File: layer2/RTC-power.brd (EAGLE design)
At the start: 17.8 x 49.5 mm, 14 parts, among them U1 DS3234, U2 MCP73831

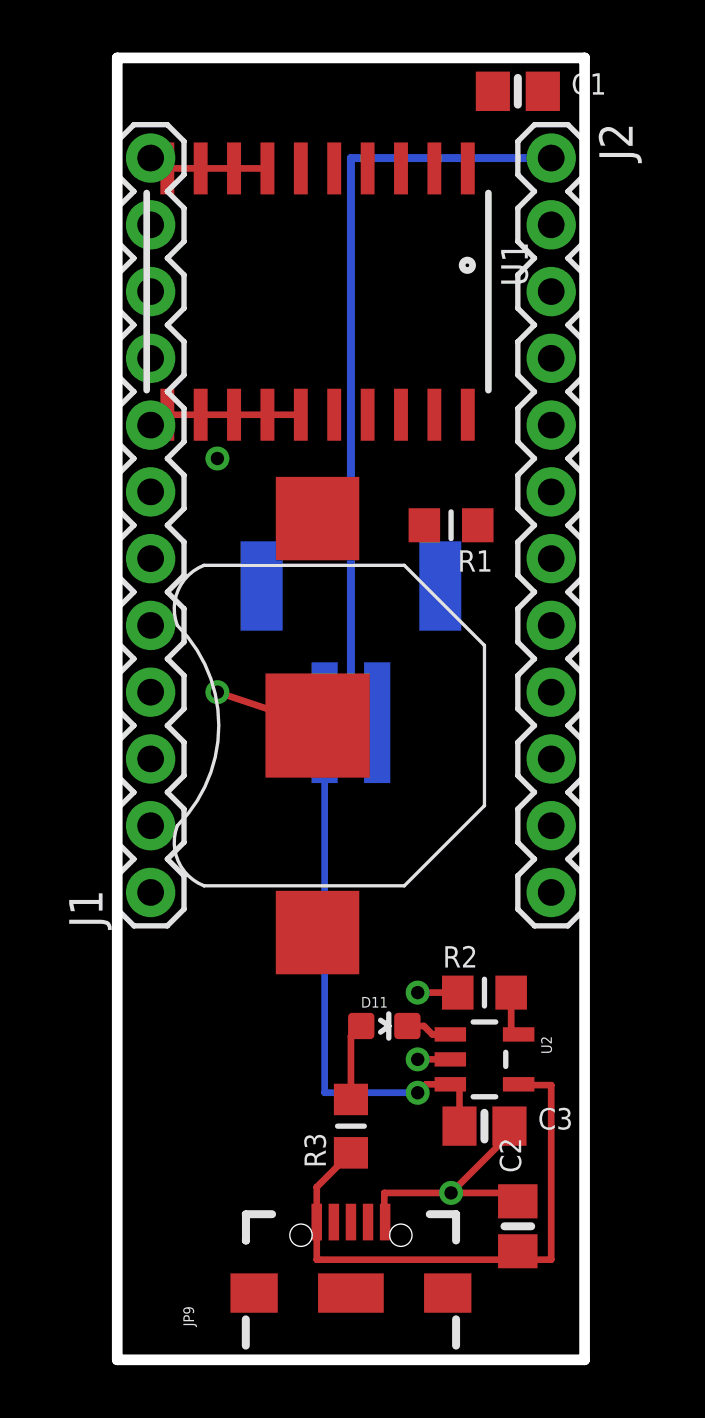
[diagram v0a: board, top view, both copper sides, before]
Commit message: layed out all conectons on board
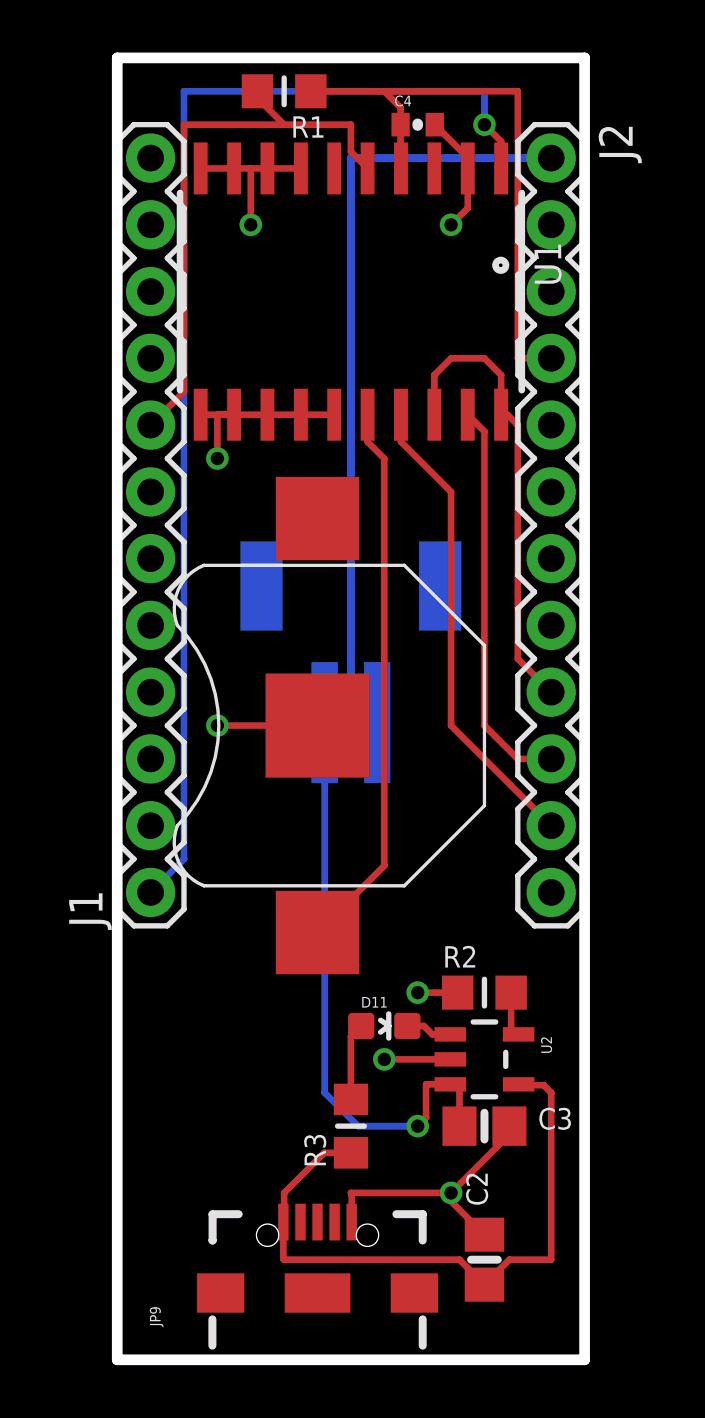
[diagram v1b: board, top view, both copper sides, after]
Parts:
- removed C1: 22pF, microbuilder:0805-NO
- added C4: 22pF, SparkFun:0402-CAP
- moved R1 17.7 mm to (6.35, 48.3)
- moved C2 1.80 mm to (14.0, 3.81)
- moved JP9 1.27 mm to (7.62, 2.54)
- moved U1 1.27 mm to (8.89, 40.6)
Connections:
- net +3V3: now also C4.1; no longer C1.1
- net GND: now also C4.2; no longer C1.2
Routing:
- net RTC_CS: track 0.00 -> 45.6 mm, vias 0 -> 1
- net +3V3: track 0.00 -> 22.5 mm
- net INT/SQW: track 0.00 -> 21.9 mm
- net RTCBATT: track 0.00 -> 21.0 mm
- net MOSI: track 0.00 -> 18.0 mm
- net SCK: track 0.00 -> 17.6 mm
- net MISO: track 0.00 -> 15.2 mm
- net GND: track 25.7 -> 36.3 mm, vias 5 -> 7
- net VIN: track 21.8 -> 24.5 mm
- net V_RAW: track 51.0 -> 52.8 mm

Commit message: replaced ground wires with top layer ground plane
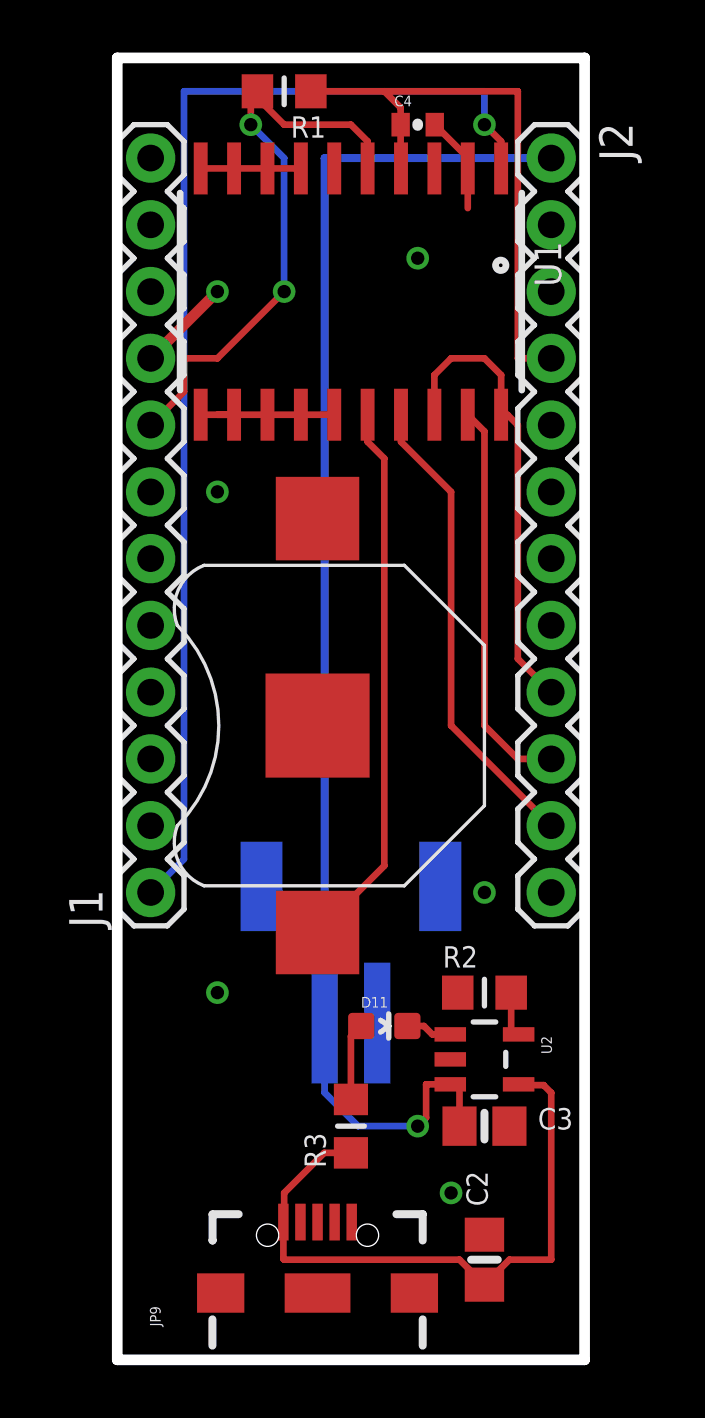
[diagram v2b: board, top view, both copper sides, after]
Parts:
- moved JP1 11.4 mm to (8.89, 16.5)
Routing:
- net GND: track 36.3 -> 16.8 mm, vias 7 -> 6
- net V_RAW: track 52.8 -> 54.2 mm
- net INT/SQW: track 21.9 -> 22.3 mm, vias 0 -> 2
- added copper zone on layer 1, net GND
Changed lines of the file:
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@@
 <element name="J1" library="SparkFun-Connectors" package="1X12" value="" x="1.27" y="17.78" rot="R90"/>
 <element name="J2" library="SparkFun-Connectors" package="1X12" value="" x="16.51" y="45.72" rot="R270"/>
-<element name="JP1" library="SparkFun-Connectors" package="JST-2-SMD@1" value="JST" x="8.89" y="27.94" rot="MR0">
-<attribute name="PROD_ID" value="CONN-08352" x="8.89" y="27.94" size="1.778" layer="28" rot="MR0" display="off"/>
+<element name="JP1" library="SparkFun-Connectors" package="JST-2-SMD@1" value="JST" x="8.89" y="16.51" rot="MR0">
+<attribute name="PROD_ID" value="CONN-08352" x="8.89" y="16.51" size="1.778" layer="28" rot="MR0" display="off"/>
 </element>
 <element name="JP9" library="SparkFun-Connectors" package="USB-AB-MICRO-SMD_V03" value="Micro USB" x="7.62" y="2.54" rot="R90">
@@
 <vertex x="17.78" y="49.53"/>
 </polygon>
-<via x="11.43" y="13.97" extent="1-16" drill="0.508"/>
-<wire x1="12.954" y1="13.97" x2="11.43" y2="13.97" width="0.254" layer="1"/>
-<wire x1="12.6699" y1="11.43" x2="10.16" y2="11.43" width="0.254" layer="1"/>
-<via x="10.16" y="11.43" extent="1-16" drill="0.508"/>
-<via x="12.7" y="6.35" extent="1-16" drill="0.508"/>
-<wire x1="8.89" y1="6.35" x2="12.7" y2="6.35" width="0.254" layer="1"/>
-<wire x1="14.92" y1="8.89" x2="14.92" y2="8.57" width="0.254" layer="1"/>
-<wire x1="14.92" y1="8.57" x2="12.7" y2="6.35" width="0.254" layer="1"/>
 <wire x1="3.175" y1="45.325" x2="4.445" y2="45.325" width="0.254" layer="1"/>
-<wire x1="4.445" y1="45.325" x2="5.08" y2="45.325" width="0.254" layer="1"/>
-<wire x1="5.08" y1="45.325" x2="5.715" y2="45.325" width="0.254" layer="1"/>
+<wire x1="4.445" y1="45.325" x2="5.715" y2="45.325" width="0.254" layer="1"/>
 <wire x1="6.985" y1="45.325" x2="5.715" y2="45.325" width="0.254" layer="1"/>
 <wire x1="8.255" y1="35.955" x2="6.985" y2="35.955" width="0.254" layer="1"/>
@@
 <wire x1="3.81" y1="35.955" x2="4.445" y2="35.955" width="0.254" layer="1"/>
 <wire x1="4.445" y1="35.955" x2="3.175" y2="35.955" width="0.254" layer="1"/>
-<via x="3.81" y="34.29" extent="1-16" drill="0.508"/>
-<wire x1="7.62" y1="24.13" x2="3.81" y2="24.13" width="0.254" layer="1"/>
-<via x="3.81" y="24.13" extent="1-16" drill="0.508"/>
-<wire x1="3.81" y1="34.29" x2="3.81" y2="35.955" width="0.254" layer="1"/>
-<via x="5.08" y="43.18" extent="1-16" drill="0.508"/>
-<wire x1="5.08" y1="43.18" x2="5.08" y2="45.325" width="0.254" layer="1"/>
-<wire x1="12.7" y1="6.35" x2="12.7" y2="6.03" width="0.254" layer="1"/>
-<wire x1="12.7" y1="6.03" x2="13.97" y2="4.76" width="0.254" layer="1"/>
-<wire x1="8.92" y1="5.24" x2="8.92" y2="6.32" width="0.254" layer="1"/>
-<wire x1="8.92" y1="6.32" x2="8.89" y2="6.35" width="0.254" layer="1"/>
+<via x="3.81" y="33.02" extent="1-16" drill="0.508"/>
 <contactref element="C4" pad="2"/>
 <wire x1="13.335" y1="45.325" x2="13.335" y2="45.735" width="0.254" layer="1"/>
 <wire x1="13.335" y1="45.735" x2="12.08" y2="46.99" width="0.254" layer="1"/>
 <wire x1="13.335" y1="45.325" x2="13.335" y2="43.815" width="0.254" layer="1"/>
-<wire x1="13.335" y1="43.815" x2="12.7" y2="43.18" width="0.254" layer="1"/>
-<via x="12.7" y="43.18" extent="1-16" drill="0.508"/>
-<wire x1="3.175" y1="35.955" x2="1.27" y2="38.1" width="0" layer="19" extent="1-1"/>
+<via x="11.43" y="41.91" extent="1-16" drill="0.508"/>
+<polygon width="0.254" layer="1" isolate="0.3048">
+<vertex x="0" y="49.53"/>
+<vertex x="17.78" y="49.53"/>
+<vertex x="17.78" y="0"/>
+<vertex x="0" y="0"/>
+</polygon>
+<via x="3.81" y="13.97" extent="1-16" drill="0.508"/>
+<via x="13.97" y="17.78" extent="1-16" drill="0.508"/>
+<via x="3.81" y="40.64" extent="1-16" drill="0.508"/>
+<wire x1="1.27" y1="38.1" x2="3.81" y2="40.64" width="0.4064" layer="1"/>
+<via x="12.7" y="6.35" extent="1-16" drill="0.508"/>
 </signal>
 <signal name="MISO">
@@
 <wire x1="5.334" y1="48.26" x2="5.334" y2="48.006" width="0.254" layer="1"/>
 <wire x1="5.334" y1="48.006" x2="6.35" y2="46.99" width="0.254" layer="1"/>
-<wire x1="8.89" y1="45.96" x2="9.525" y2="45.325" width="0.254" layer="1"/>
-<wire x1="6.35" y1="46.99" x2="2.54" y2="46.99" width="0.254" layer="1"/>
-<wire x1="2.54" y1="46.99" x2="2.54" y2="36.83" width="0.254" layer="1"/>
-<wire x1="2.54" y1="36.83" x2="1.27" y2="35.56" width="0.254" layer="1"/>
 <wire x1="6.35" y1="46.99" x2="8.89" y2="46.99" width="0.254" layer="1"/>
-<wire x1="8.89" y1="46.99" x2="8.89" y2="45.96" width="0.254" layer="1"/>
+<wire x1="9.525" y1="45.325" x2="9.525" y2="46.355" width="0.254" layer="1"/>
+<wire x1="9.525" y1="46.355" x2="8.89" y2="46.99" width="0.254" layer="1"/>
+<wire x1="1.27" y1="35.56" x2="2.54" y2="36.83" width="0.254" layer="1"/>
+<wire x1="2.54" y1="36.83" x2="2.54" y2="38.1" width="0.254" layer="1"/>
+<wire x1="2.54" y1="38.1" x2="3.81" y2="38.1" width="0.254" layer="1"/>
+<wire x1="3.81" y1="38.1" x2="6.35" y2="40.64" width="0.254" layer="1"/>
+<via x="6.35" y="40.64" extent="1-16" drill="0.508"/>
+<wire x1="6.35" y1="40.64" x2="6.35" y2="45.72" width="0.254" layer="16"/>
+<wire x1="6.35" y1="45.72" x2="5.08" y2="46.99" width="0.254" layer="16"/>
+<via x="5.08" y="46.99" extent="1-16" drill="0.508"/>
+<wire x1="5.08" y1="46.99" x2="5.08" y2="48.006" width="0.254" layer="1"/>
+<wire x1="5.08" y1="48.006" x2="5.334" y2="48.26" width="0.254" layer="1"/>
 </signal>
 <signal name="RTCBATT">
@@
 <wire x1="12.6699" y1="10.48" x2="11.75" y2="10.48" width="0.254" layer="1"/>
 <via x="11.43" y="8.89" extent="1-16" drill="0.508"/>
-<wire x1="7.89" y1="10.16" x2="7.89" y2="24.24" width="0.254" layer="16"/>
-<wire x1="7.89" y1="24.24" x2="8.89" y2="24.24" width="0.3048" layer="16"/>
-<wire x1="8.89" y1="24.24" x2="8.89" y2="45.72" width="0.3048" layer="16"/>
-<wire x1="16.51" y1="45.72" x2="8.89" y2="45.72" width="0.3048" layer="16"/>
+<wire x1="7.89" y1="10.16" x2="7.89" y2="11.43" width="0.254" layer="16"/>
+<wire x1="7.89" y1="11.43" x2="7.89" y2="12.81" width="0.254" layer="16"/>
 <wire x1="11.75" y1="10.48" x2="11.75" y2="9.21" width="0.254" layer="1"/>
 <wire x1="11.75" y1="9.21" x2="11.43" y2="8.89" width="0.254" layer="1"/>
 <wire x1="11.43" y1="8.89" x2="9.16" y2="8.89" width="0.254" layer="16"/>
 <wire x1="9.16" y1="8.89" x2="7.89" y2="10.16" width="0.254" layer="16"/>
+<wire x1="16.51" y1="45.72" x2="7.89" y2="45.72" width="0.3048" layer="16"/>
+<wire x1="7.89" y1="45.72" x2="7.89" y2="11.43" width="0.3048" layer="16"/>
 </signal>
 <signal name="N$1">

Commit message: removed unneeded header to give battery access
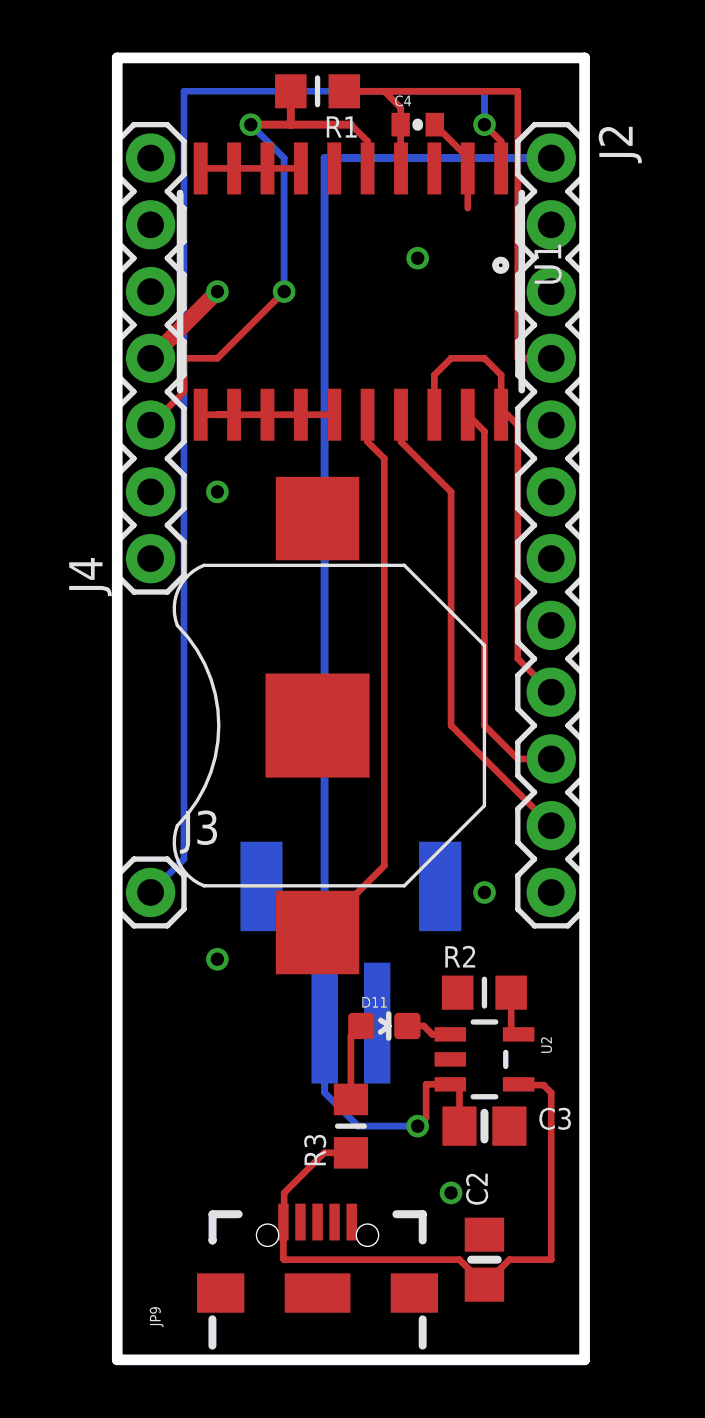
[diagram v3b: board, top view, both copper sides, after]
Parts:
- removed J1: (no value), SparkFun-Connectors:1X12
- added J3: (no value), SparkFun-Connectors:1X01
- added J4: (no value), SparkFun-Connectors:1X07
- moved R1 1.27 mm to (7.62, 48.3)
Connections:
- net GND: now also J4.4; no longer J1.9
- net INT/SQW: now also J4.3; no longer J1.8
- net RTC_CS: now also J3.1; no longer J1.1
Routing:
- net +3V3: track 22.5 -> 21.2 mm
- net INT/SQW: track 22.3 -> 21.8 mm
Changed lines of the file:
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@@
 <attribute name="PROD_ID" value="DIO-00819" x="10.16" y="12.7" size="1.778" layer="27" rot="R270" display="off"/>
 </element>
-<element name="J1" library="SparkFun-Connectors" package="1X12" value="" x="1.27" y="17.78" rot="R90"/>
 <element name="J2" library="SparkFun-Connectors" package="1X12" value="" x="16.51" y="45.72" rot="R270"/>
 <element name="JP1" library="SparkFun-Connectors" package="JST-2-SMD@1" value="JST" x="8.89" y="16.51" rot="MR0">
@@
 <attribute name="PROD_ID" value="IC-09995" x="13.97" y="11.43" size="1.778" layer="27" rot="R270" display="off"/>
 </element>
-<element name="R1" library="microbuilder" package="_0805MP" value="10K" x="6.35" y="48.26" rot="R180"/>
+<element name="R1" library="microbuilder" package="_0805MP" value="10K" x="7.62" y="48.26" rot="R180"/>
 <element name="R3" library="microbuilder" package="_0805MP" value="330" x="8.89" y="8.89" rot="R90"/>
 <element name="R2" library="microbuilder" package="_0805MP" value="2.0k" x="13.97" y="13.97"/>
@@
 <element name="C3" library="microbuilder" package="0805-NO" value="4.7uF" x="13.97" y="8.89"/>
 <element name="C4" library="SparkFun" package="0402-CAP" value="22pF" x="11.43" y="46.99"/>
+<element name="J3" library="SparkFun-Connectors" package="1X01" value="" x="1.27" y="17.78"/>
+<element name="J4" library="SparkFun-Connectors" package="1X07" value="" x="1.27" y="30.48" rot="R90"/>
 </elements>
 <signals>
 <signal name="RTC_CS">
 <contactref element="U1" pad="1"/>
-<contactref element="J1" pad="1"/>
 <via x="13.97" y="46.99" extent="1-16" drill="0.508"/>
 <wire x1="13.97" y1="46.99" x2="13.97" y2="48.26" width="0.254" layer="16"/>
@@
 <wire x1="14.605" y1="45.325" x2="14.605" y2="46.355" width="0.254" layer="1"/>
 <wire x1="14.605" y1="46.355" x2="13.97" y2="46.99" width="0.254" layer="1"/>
+<contactref element="J3" pad="1"/>
 </signal>
 <signal name="GND">
@@
 <contactref element="JP9" pad="GND1"/>
 <contactref element="JP1" pad="1"/>
-<contactref element="J1" pad="9"/>
 <contactref element="J2" pad="2"/>
 <contactref element="R2" pad="1"/>
@@
 <vertex x="0" y="0"/>
 </polygon>
-<via x="3.81" y="13.97" extent="1-16" drill="0.508"/>
+<via x="3.81" y="15.24" extent="1-16" drill="0.508"/>
 <via x="13.97" y="17.78" extent="1-16" drill="0.508"/>
 <via x="3.81" y="40.64" extent="1-16" drill="0.508"/>
-<wire x1="1.27" y1="38.1" x2="3.81" y2="40.64" width="0.4064" layer="1"/>
+<wire x1="1.27" y1="38.1" x2="3.81" y2="40.64" width="0.6096" layer="1"/>
 <via x="12.7" y="6.35" extent="1-16" drill="0.508"/>
+<contactref element="J4" pad="4"/>
 </signal>
 <signal name="MISO">
@@
 <signal name="INT/SQW">
 <contactref element="U1" pad="5"/>
-<contactref element="J1" pad="8"/>
 <contactref element="R1" pad="2"/>
-<wire x1="5.334" y1="48.26" x2="5.334" y2="48.006" width="0.254" layer="1"/>
-<wire x1="5.334" y1="48.006" x2="6.35" y2="46.99" width="0.254" layer="1"/>
-<wire x1="6.35" y1="46.99" x2="8.89" y2="46.99" width="0.254" layer="1"/>
 <wire x1="9.525" y1="45.325" x2="9.525" y2="46.355" width="0.254" layer="1"/>
 <wire x1="9.525" y1="46.355" x2="8.89" y2="46.99" width="0.254" layer="1"/>
@@
 <wire x1="6.35" y1="45.72" x2="5.08" y2="46.99" width="0.254" layer="16"/>
 <via x="5.08" y="46.99" extent="1-16" drill="0.508"/>
-<wire x1="5.08" y1="46.99" x2="5.08" y2="48.006" width="0.254" layer="1"/>
-<wire x1="5.08" y1="48.006" x2="5.334" y2="48.26" width="0.254" layer="1"/>
+<wire x1="8.89" y1="46.99" x2="6.604" y2="46.99" width="0.3048" layer="1"/>
+<wire x1="6.604" y1="46.99" x2="6.604" y2="48.26" width="0.3048" layer="1"/>
+<wire x1="6.604" y1="46.99" x2="5.08" y2="46.99" width="0.3048" layer="1"/>
+<contactref element="J4" pad="3"/>
 </signal>
 <signal name="RTCBATT">
@@
 <wire x1="15.24" y1="38.1" x2="15.24" y2="48.26" width="0.254" layer="1"/>
 <contactref element="C4" pad="1"/>
-<wire x1="7.366" y1="48.26" x2="10.16" y2="48.26" width="0.254" layer="1"/>
+<wire x1="8.636" y1="48.26" x2="10.16" y2="48.26" width="0.254" layer="1"/>
 <wire x1="10.16" y1="48.26" x2="15.24" y2="48.26" width="0.254" layer="1"/>
 <wire x1="10.78" y1="46.99" x2="10.78" y2="45.34" width="0.254" layer="1"/>
